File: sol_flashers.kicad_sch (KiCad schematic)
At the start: 36 parts, among them J125 J125 Sol 17-24 drive (backbox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, J126 J126 Sol 17-24 drive (playfie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, Q28 IRLR3110ZTRPBF, Q30 IRLR3110ZTRPBF, Q32 IRLR3110ZTRPBF, Q34 IRLR3110ZTRPBF, Q36 IRLR3110ZTRPBF, Q38 IRLR3110ZTRPBF, Q40 IRLR3110ZTRPBF, Q42 IRLR3110ZTRPBF, U3 74HCT574

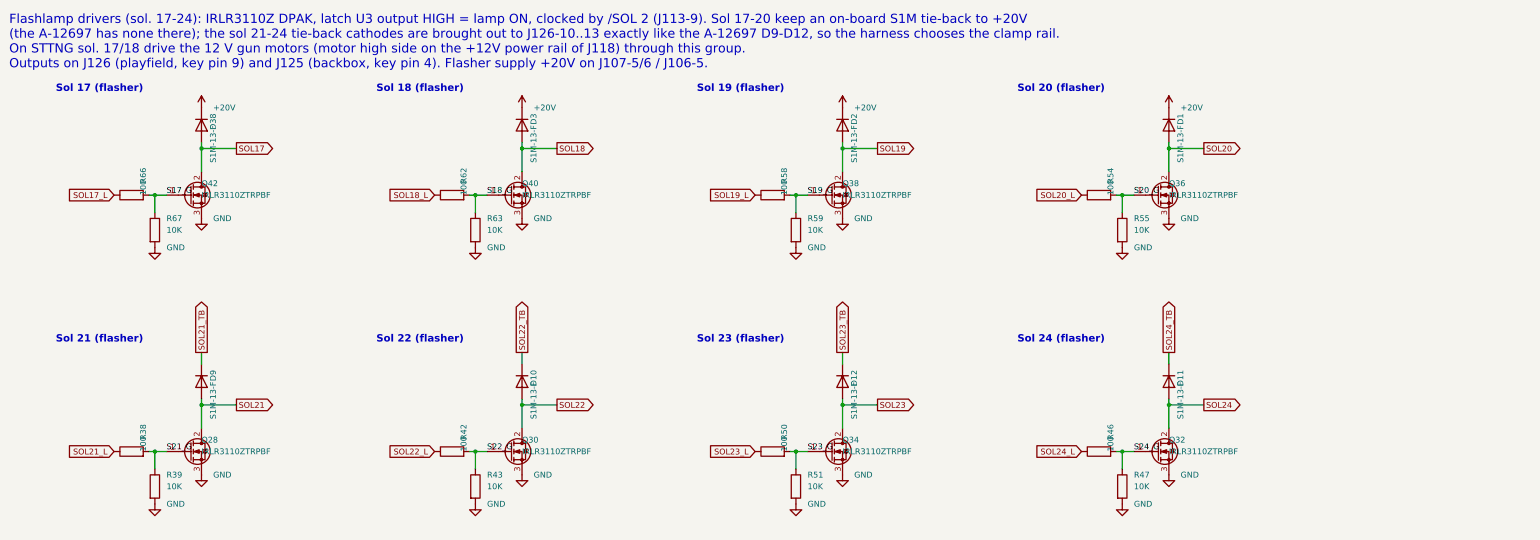
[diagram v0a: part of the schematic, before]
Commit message: Prepare WPC engineering candidate and verification tooling
Include revised PCB and schematics, component models, fabrication exports, renders, BOM, assembly counts, and reproducible electrical and manufacturing checks. Document unresolved replay convergence, regulator fault behavior, and physical qualification gates; this candidate is not production released.
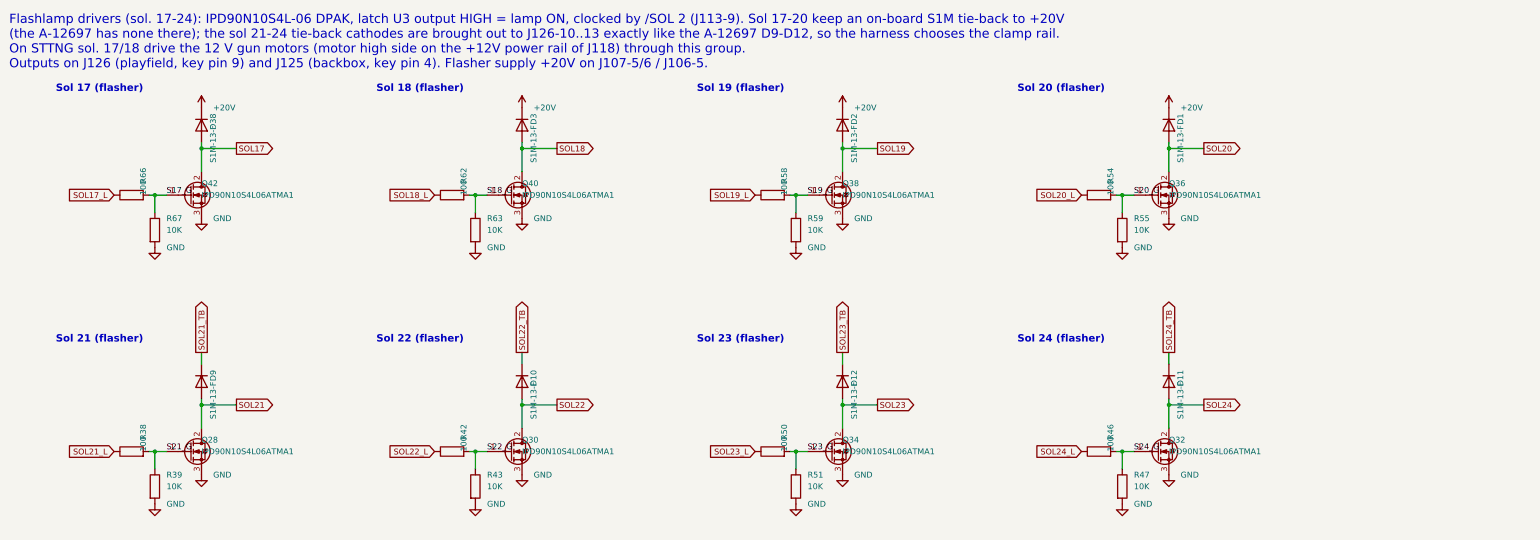
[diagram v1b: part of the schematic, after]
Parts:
- B3: symbol Device:C -> wpc_symbols:Device_C
- D1, D10, D11, D12, D2, D3, D38, D9: symbol Diode:1N4007 -> wpc_symbols:Diode_1N4007
- J125: symbol Connector_Generic:Conn_01x09 -> wpc_symbols:Connector_Generic_Conn_01x09; MPN 0026604009 -> 0026604090
- J126: symbol Connector_Generic:Conn_01x13 -> wpc_symbols:Connector_Generic_Conn_01x13; Link https://www.digikey.com/en/products/result?keywords=0026604013 -> https://www.digikey.com/en/products/result?keywords=0026604130; MPN 0026604013 -> 0026604130
- Q28, Q30, Q32, Q34, Q36, Q38, Q40, Q42: value IRLR3110ZTRPBF -> IPD90N10S4L06ATMA1; symbol Transistor_FET:Q_NMOS_GDS -> wpc_symbols:Transistor_FET_Q_NMOS_GDS; Link https://www.digikey.com/en/products/detail/infineon-technol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 -> https://www.infineon.com/part/IPD90N10S4L-06; MPN IRLR3110ZTRPBF -> IPD90N10S4L06ATMA1
- R38, R39, R42, R43, R46, R47, R50, R51, R54, R55, R58, R59, R62, R63, R66, R67: symbol Device:R -> wpc_symbols:Device_R
- U3: symbol 74xx:74HCT574 -> wpc_symbols:74xx_74HCT574
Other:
- note added: "Flashlamp drivers (sol. 17-24): IPD90N10S4L-06 DPAK, latch U3 output HIGH = lamp ON, clocked by /SOL 2 (J113-9). Sol 17-20 keep an on-board S1M tie-back to +20V (the A-12697 has none there); the sol 21-24 tie-back cathodes are brought out to J126-10..13 exactly like the A-12697 D9-D12, so the harness chooses the clamp rail. On STTNG sol. 17/18 drive the 12 V gun motors (motor high side on the +12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"
- note removed: "Flashlamp drivers (sol. 17-24): IRLR3110Z DPAK, latch U3 output HIGH = lamp ON, clocked by /SOL 2 (J113-9). Sol 17-20 keep an on-board S1M tie-back to +20V (the A-12697 has none there); the sol 21-24 tie-back cathodes are brought out to J126-10..13 exactly like the A-12697 D9-D12, so the harness chooses the clamp rail. On STTNG sol. 17/18 drive the 12 V gun motors (motor high side on the +12V pow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"
- title: Solenoids 17-24 (flashlamps, IRLR3110Z) -> Solenoids 17-24 (flashlamps, IPD90N10S4L-06)
